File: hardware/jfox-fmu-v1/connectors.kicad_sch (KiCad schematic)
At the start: 4 parts, among them J12 CAN1, J13 CAN2, J40 DF12C3.0-60DS, J6 DEBUG

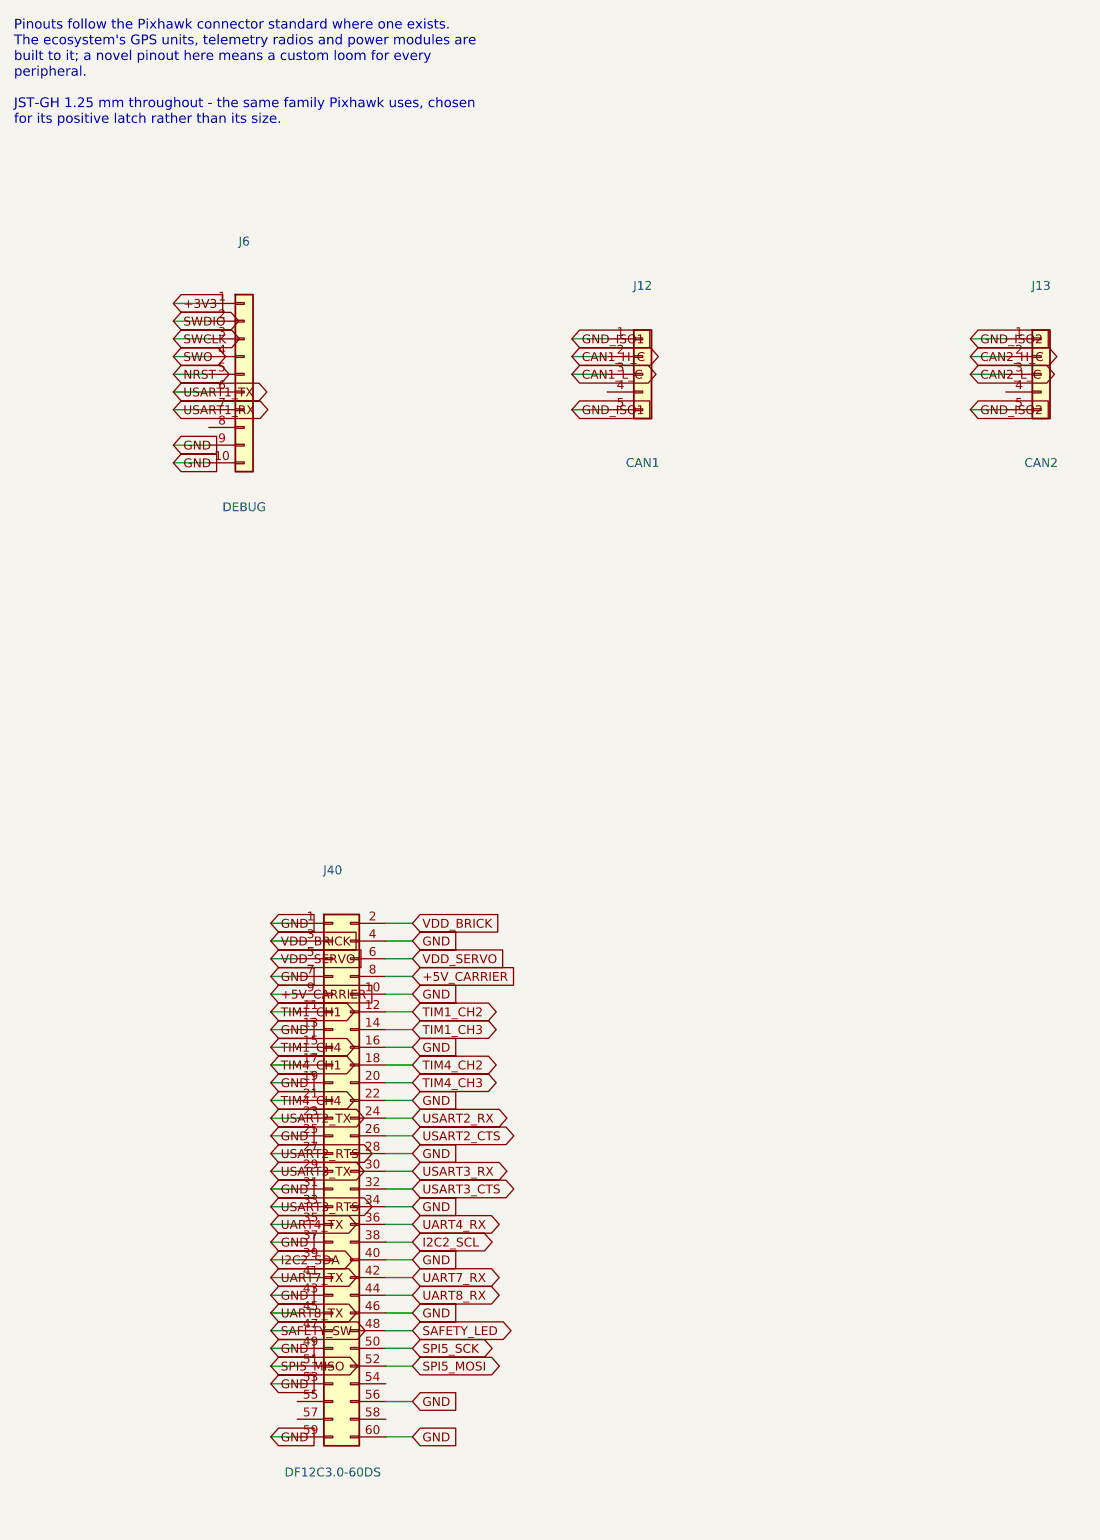
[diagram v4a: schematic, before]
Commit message: Card-cage TMR: FCU becomes a plug-in card, backplane carries the I/O
The FMU stops being a module that mates face-to-face with a base board
underneath it and becomes a card that slides into a backplane. That change
came from the JFOX FCU V1 sketch, and it dissolved a constraint I had
worked around rather than removed: the DF12 mezzanine's 3.0 mm stack height
joins two adjacent boards only, so three channels each needing an
independent path to one base board could not use it. Riser cards were the
workaround. Mating at the card's rear edge means nothing has to span the
gap, so the risers and their extra mated pair per channel are gone.

FCU card, 40 x 90 mm (was 100 x 80):
  * 58-contact Samtec MECF-30 card edge, polarised. Contacts 21/22 are a
    1.24 x 7.0 mm key notch offset from centre - a card the wrong way round
    physically will not enter, which is the only insertion safeguard that
    works before power is applied. Two grounds were sacrificed for it out of
    twenty rather than any signal.
  * Power input tree (LTC4417, six ORing FETs, dividers, input TVS) and the
    debug header move to the backplane. The card receives an already-ORed,
    already-fused +5V_CARRIER on three fingers.
  * Front edge carries everything a person touches: microSD, USB-C, and two
    lamps flanking it. D1 is hardwired to the rail so it lights with no
    firmware running - a power lamp the MCU drives tells you the MCU is
    alive, which is not what anyone reads it for.
  * Power and isolated blocks moved to the back face. Both noise groups are
    grouped at one end so the sensor island can sit 22 mm clear at the
    other; spread out, every point on an 80 mm body is within 13 mm of
    something switching.

JFOX-BASE-v1 backplane, 100 x 100 mm, new:
  * Three independent card-edge sockets in a column. A bent contact in one
    slot costs one channel; a shared bus would cost all three and leave the
    voter nothing to vote on.
  * Two airframe feeds at opposite corners, ORed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
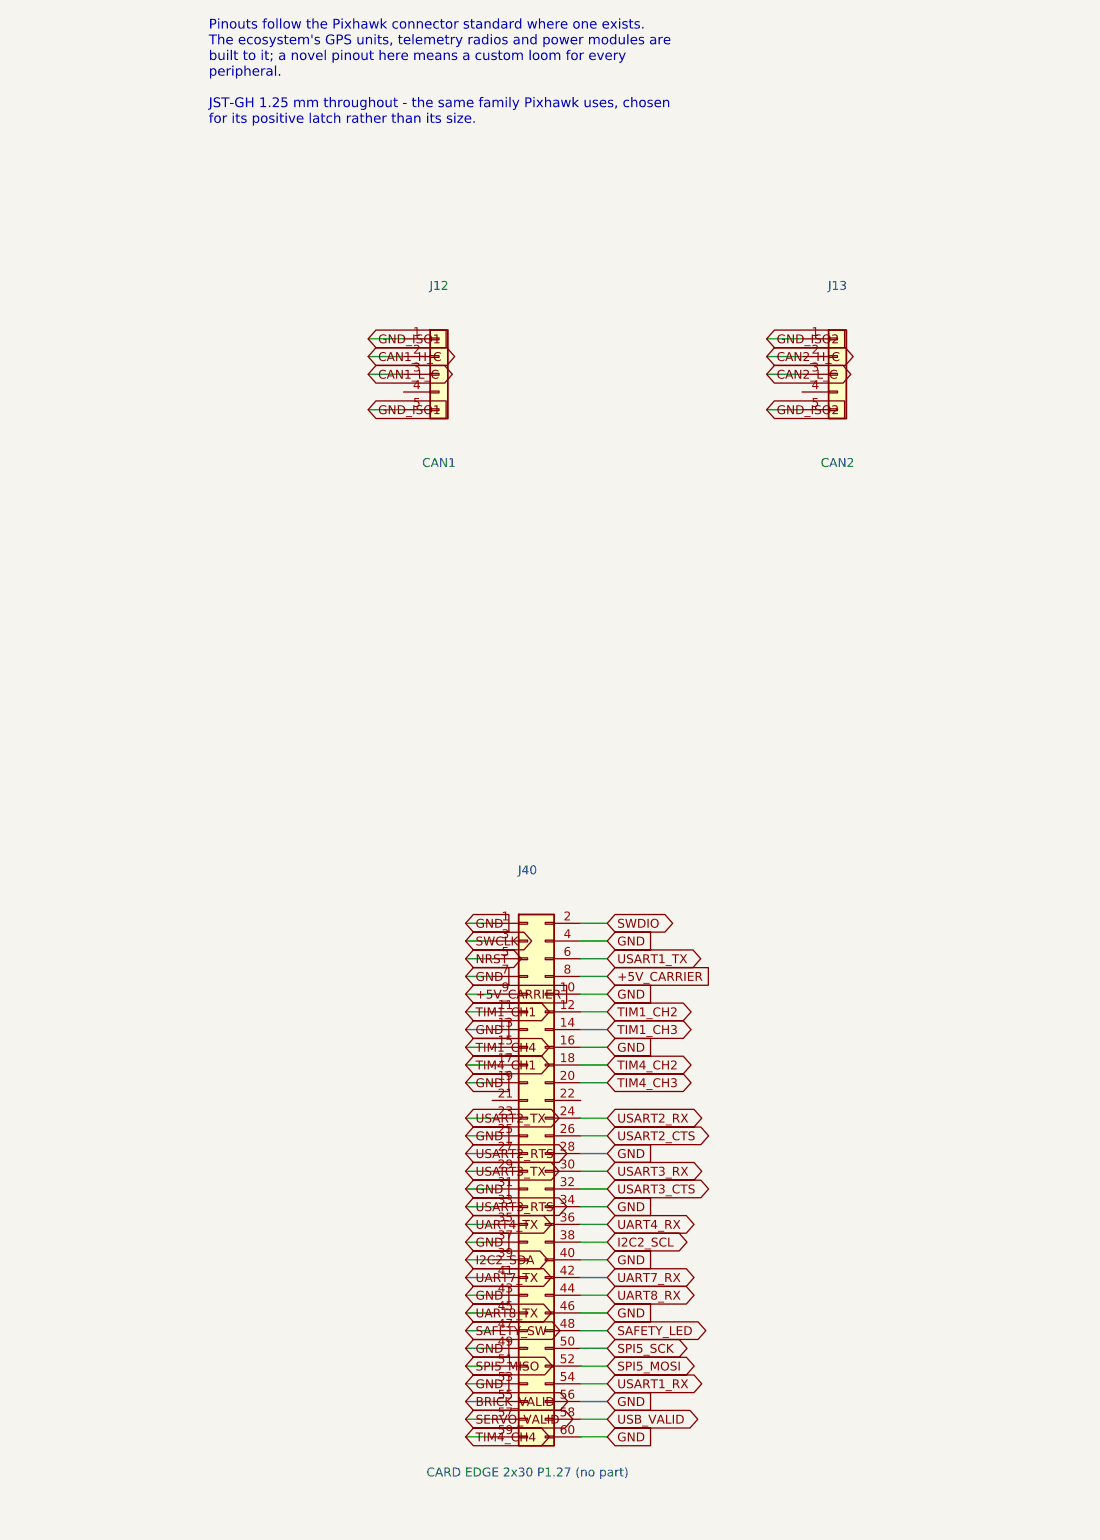
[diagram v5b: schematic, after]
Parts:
- removed J6: DEBUG, Connector_JST:JST_GH_SM10B-GHS-TB_1x10-1MP_P1.25mm_Horizontal, symbol Connector_Generic:Conn_01x10
- J40: value DF12C3.0-60DS -> CARD EDGE 2x30 P1.27 (no part); footprint Connector_Hirose:Hirose_DF12_DF12C3.0-60DS-0.5V_2x30_P0.50mm_Vertical -> Connector_PCBEdge:Samtec_MECF-30-0_-L-DV_2x30_P1.27mm_Polarized_Edge
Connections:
- net GND: no longer J40.22 (Pin_22), J40.59 (Pin_59)
- net NRST: now also J40.5 (Pin_5)
- net SWCLK: now also J40.3 (Pin_3)
- net SWDIO: now also J40.2 (Pin_2)
- net TIM4_CH4: now also J40.59 (Pin_59); no longer J40.21 (Pin_21)
- net USART1_RX: now also J40.54 (Pin_54)
- net USART1_TX: now also J40.6 (Pin_6)
- net BRICK_VALID: now reaches J40.55 (Pin_55)
- net SERVO_VALID: now reaches J40.57 (Pin_57)
- net USB_VALID: now reaches J40.58 (Pin_58)
- removed net VDD_BRICK: J40.2 (Pin_2), J40.3 (Pin_3)
- removed net VDD_SERVO: J40.5 (Pin_5), J40.6 (Pin_6)

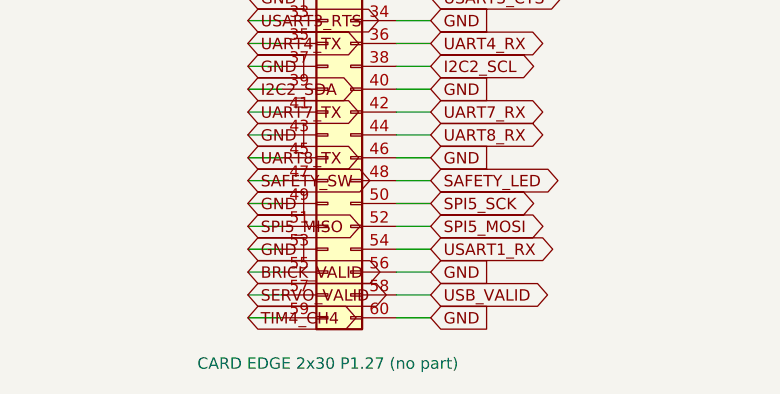
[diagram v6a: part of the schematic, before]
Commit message: Provability: check the backplane, and fix the four defects that found
Nothing read JFOX-BASE-v1. Every checker in hardware/tools/ opened
jfox-fmu-v1/jfox-fmu.kicad_sch and only that, so no claim about the
backplane was provable - including the ones the requirements table recorded
as verified.

check_base_schematic.py now reads it: fused rails must reach a card socket,
the LTC4417 divider must produce the window it claims, that window must fit
every part downstream, and the feed-health outputs must reach a card AND be
driven. It failed on first run, which is the only reason to trust it.

What it found, in the order it found them:

  1. THE CARDS HAD NO POWER. The fuses put out A/B/C_FUSED and the card edge
     reads +5V_CARRIER. Both boards generated cleanly, both passed DRC, and
     the two halves were never connected to each other. The chain now
     terminates on the card rail past the shunt, not before it.

  2. THE FEEDS ARE NOT BATTERIES. VBAT_RH/VBAT_LH carry 5 V - the thresholds
     said so and the connectors are labelled PWR. Renamed PWR1_IN/PWR2_IN,
     output PWR_ORED. The name was the thing that was wrong.

  3. THE WINDOW PASSED MORE THAN A PART SURVIVES, and the binding part was
     not the one found by hand. The analysis flagged the AP2112K at 6.0 V
     against a 5.81 V threshold - 190 mV. The checker compared against every
     downstream part and found the ISOW1044 at 5.5 V: NEGATIVE 310 mV. A
     feed the controller reported as good would have destroyed the isolator.

     787k / 28k7 / 196k -> UV 4.50 V, OV 5.16 V
       ISOW1044  +338 mV      AP2112K  +838 mV

  4. THE ORING CONTROLLER'S OUTPUT WAS NEVER CONNECTED. Its pin map was
     written from the datasheet's block diagram, not the symbol: the pins
     are ~{VALID1..3} with overbars, VOUT not OUT, HYS not HYST, and there
     is no STAT pin at all. nets.get() returns None for an unknown key, so
     six pins were silently left unwired - VOUT among them. PWR_ORED was fed
     only by D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
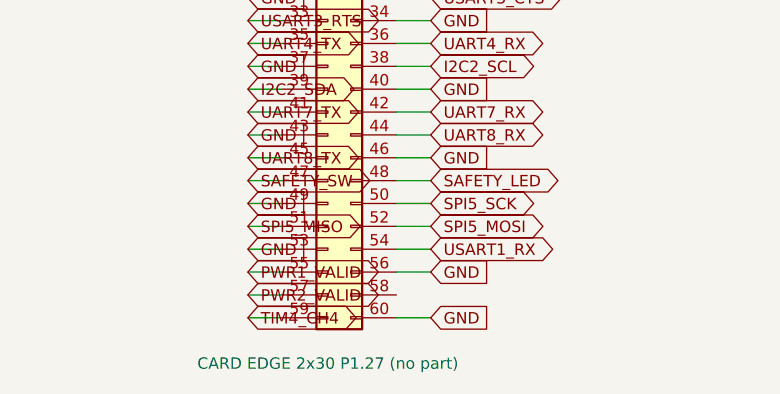
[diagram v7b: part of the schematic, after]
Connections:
- net BRICK_VALID renamed PWR1_VALID
- net SERVO_VALID renamed PWR2_VALID
- net USB_VALID: no longer names the net of J40.58 (Pin_58)
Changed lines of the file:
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@@
 		(instances
 			(project "jfox-fmu"
-				(path "/8d360e86-1eb2-4a7a-9344-46638f0c46a3"
+				(path "/0b2951fc-7dfb-4148-a219-9f8c1f782ac7"
 					(reference "J12")
 					(unit 1)
@@
 		(instances
 			(project "jfox-fmu"
-				(path "/8d360e86-1eb2-4a7a-9344-46638f0c46a3"
+				(path "/0b2951fc-7dfb-4148-a219-9f8c1f782ac7"
 					(reference "J13")
 					(unit 1)
@@
 		(instances
 			(project "jfox-fmu"
-				(path "/8d360e86-1eb2-4a7a-9344-46638f0c46a3"
+				(path "/0b2951fc-7dfb-4148-a219-9f8c1f782ac7"
 					(reference "J40")
 					(unit 1)
@@
 		)
 	)
-	(global_label "BRICK_VALID"
+	(global_label "PWR1_VALID"
 		(shape bidirectional)
 		(at 96.52 212.09 0)
@@
 		)
 	)
-	(global_label "SERVO_VALID"
+	(global_label "PWR2_VALID"
 		(shape bidirectional)
 		(at 96.52 214.63 0)
 		(fields_autoplaced yes)
 		(effects
-			(font
-				(size 1.27 1.27)
-			)
-			(justify left)
-		)
-	)
-	(wire
-		(pts
-			(xy 113.03 214.63) (xy 116.84 214.63)
-		)
-		(stroke
-			(width 0)
-			(type default)
-		)
-	)
-	(global_label "USB_VALID"
-		(shape bidirectional)
-		(at 116.84 214.63 180)
-		(fields_autoplaced yes)
-		(effects
